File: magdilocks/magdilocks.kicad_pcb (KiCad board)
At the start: 2 copper layers, 13.9 x 10.8 mm, 11 parts, among them J1 Conn_1x3, J2 Conn_1x3, J3 Conn_1x3, U1 U_DRV5053, U2 U_Si7210

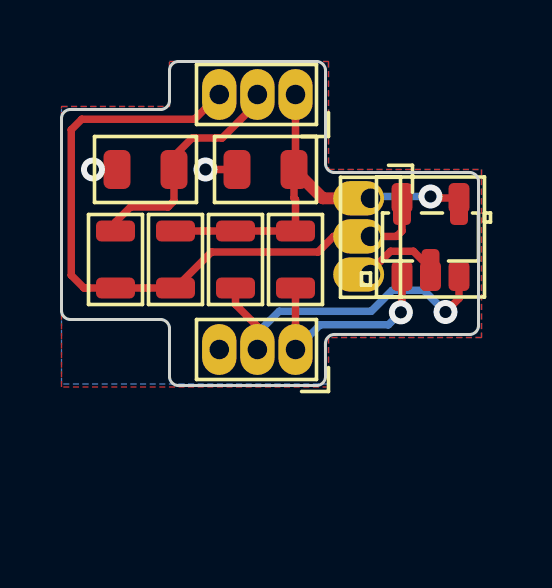
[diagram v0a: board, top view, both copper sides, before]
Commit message: v2.0 Release
Modified board shape to fit on Phob 1.2.2. Changed pin assignments for development headers.
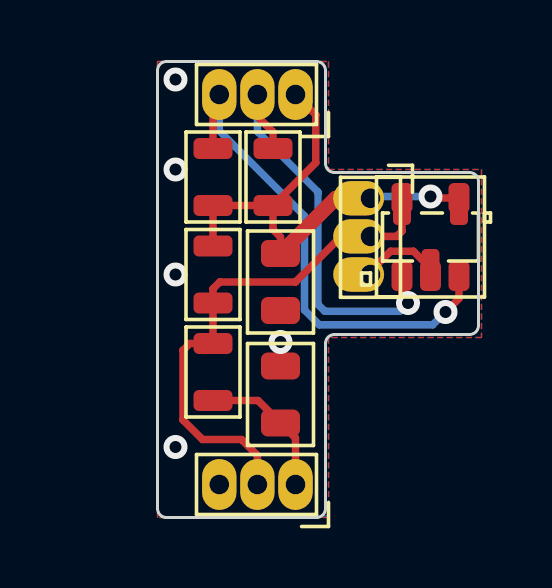
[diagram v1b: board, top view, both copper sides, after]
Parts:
- moved J2 13.0 mm to (97.5, 132.0)
- moved C1 8.75 mm to (97.0, 129.0), turned to 90 degrees
- moved J3 8.50 mm to (97.5, 119.0)
- moved R4 4.96 mm to (94.8, 128.2), turned to -90 degrees
- moved C2 3.78 mm to (97.0, 125.2), turned to -90 degrees
- moved R2 2.85 mm to (94.8, 121.8), turned to 90 degrees
- moved R3 2.85 mm to (96.8, 121.8), turned to 90 degrees
- moved R1 1.35 mm to (94.8, 125.0)
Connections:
- J2 pad 1: +3V3 -> /OUT_FLT
- J2 pad 2: /OUT_FLT -> /OUT_RAW
- J2 pad 3: /OUT_RAW -> GND
- J3 pad 1: /SDA -> +3V3
- J3 pad 2: /SCL -> /SDA
- J3 pad 3: GND -> /SCL
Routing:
- net /SDA: track 7.30 -> 14.0 mm
- net /OUT_RAW: track 23.1 -> 17.1 mm
- net /SCL: track 11.4 -> 16.7 mm
- net /OUT_FLT: track 7.83 -> 4.82 mm
- net GND: track 4.98 -> 3.12 mm, vias 2 -> 5
- net +3V3: track 15.0 -> 16.7 mm
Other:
- board size 13.9 x 10.8 mm -> 10.7 x 15.2 mm

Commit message: V2.0 production release
Fixed board shape to fit main board and c-stick PBCs. Created gerber/drill files, BOM export, 3D model, and render examples on Phob 1.2.2.
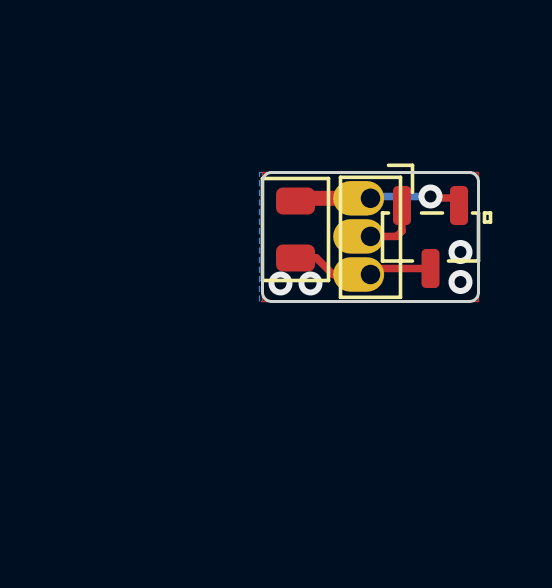
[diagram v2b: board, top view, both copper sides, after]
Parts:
- removed C1: C, master-vampire:C_0805
- removed J2, J3: Conn_1x3, master-vampire:CONN_HEADER_MALE_1X3PIN_P1.27MM_TH
- removed R1, R2, R3, R4: R, master-vampire:R_0805
- removed U2: U_Si7210, master-vampire:SOT-23-5
- moved C2 1.82 mm to (97.5, 123.5)
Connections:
- net /OUT_RAW renamed Net-(J1-Pad2)
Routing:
- net /SCL: track 16.7 -> 0.00 mm, vias 1 -> 0
- net Net-(J1-Pad2): track 17.1 -> 2.95 mm
- net /SDA: track 14.0 -> 0.00 mm, vias 1 -> 0
- net +3V3: track 16.7 -> 6.14 mm
- net /OUT_FLT: track 4.82 -> 0.00 mm
- net GND: track 3.12 -> 5.12 mm, vias 5 -> 4
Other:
- board size 10.7 x 15.2 mm -> 7.2 x 4.3 mm
- board text removed: "3V3"
- board text removed: "FLT"
- board text removed: "GND"
- board text removed: "RAW"
- board text removed: "SCL"
- board text removed: "SDA"
